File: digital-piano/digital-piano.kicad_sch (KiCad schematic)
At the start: 20 parts, among them J1 Conn_01x22, J10 Conn_01x01, J11 Conn_01x01, J12 Conn_01x01, J13 Conn_01x01, J14 Conn_01x01, J15 Conn_01x01, J16 Conn_01x01, J2 Conn_01x22, J3 Conn_01x01, J4 Conn_01x01, J5 Conn_01x01, J6 Conn_01x01, J7 Conn_01x01, J8 Conn_01x01, J9 Conn_01x01

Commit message: Assign footprints to digital-piano
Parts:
- S4: Availability In Stock -> (none); Check_prices https://www.snapeda.com/parts/SKRPACE010/ALPS/view-part/?re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 -> (none); Description_1 Switch Tactile N.O. SPST Button J-Bend 0.05A 16VDC 2.55N SM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 -> (none); MANUFACTURER ALPS -> (none); MF ALPS -> (none); MP SKRPACE010 -> (none); Package None -> (none); Price None -> (none); STANDARD Maniufacturer Recommendations -> (none); SnapEDA_Link https://www.snapeda.com/parts/SKRPACE010/ALPS/view-part/?re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 -> (none)
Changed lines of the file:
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@@
 			)
 		)
-		(property "MF" "ALPS"
+		(property "MF" ""
 			(at 232.41 114.3 0)
 			(effects
@@
 			)
 		)
-		(property "Description_1" "\n                        \n                            Switch Tactile N.O. SPST Button J-Bend 0.05A 16VDC 2.55N SMD Automotive T/R\n                        \n"
+		(property "Description_1" ""
 			(at 232.41 114.3 0)
 			(effects
@@
 			)
 		)
-		(property "Package" "None"
+		(property "Package" ""
 			(at 232.41 114.3 0)
 			(effects
@@
 			)
 		)
-		(property "Price" "None"
+		(property "Price" ""
 			(at 232.41 114.3 0)
 			(effects
@@
 			)
 		)
-		(property "Check_prices" "https://www.snapeda.com/parts/SKRPACE010/ALPS/view-part/?ref=eda"
+		(property "Check_prices" ""
 			(at 232.41 114.3 0)
 			(effects
@@
 			)
 		)
-		(property "STANDARD" "Maniufacturer Recommendations"
+		(property "STANDARD" ""
 			(at 232.41 114.3 0)
 			(effects
@@
 			)
 		)
-		(property "SnapEDA_Link" "https://www.snapeda.com/parts/SKRPACE010/ALPS/view-part/?ref=snap"
+		(property "SnapEDA_Link" ""
 			(at 232.41 114.3 0)
 			(effects
@@
 			)
 		)
-		(property "MP" "SKRPACE010"
+		(property "MP" ""
 			(at 232.41 114.3 0)
 			(effects
@@
 			)
 		)
-		(property "Availability" "In Stock"
+		(property "Availability" ""
 			(at 232.41 114.3 0)
 			(effects
@@
 			)
 		)
-		(property "MANUFACTURER" "ALPS"
+		(property "MANUFACTURER" ""
 			(at 232.41 114.3 0)
 			(effects

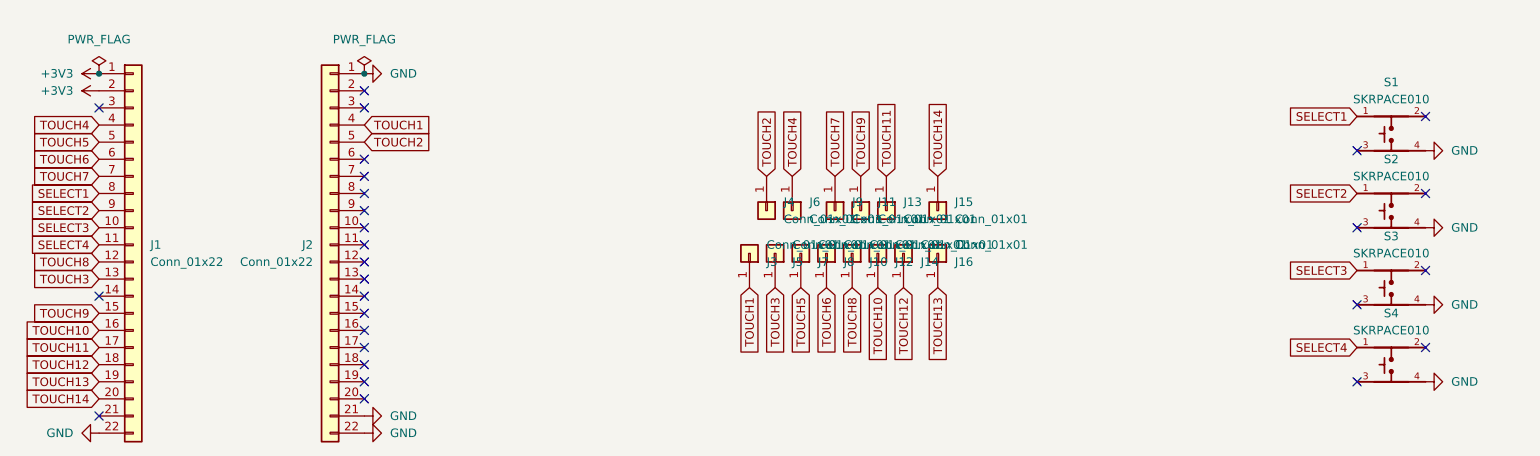
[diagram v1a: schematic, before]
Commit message: Change the name of the footprint library of touchpad
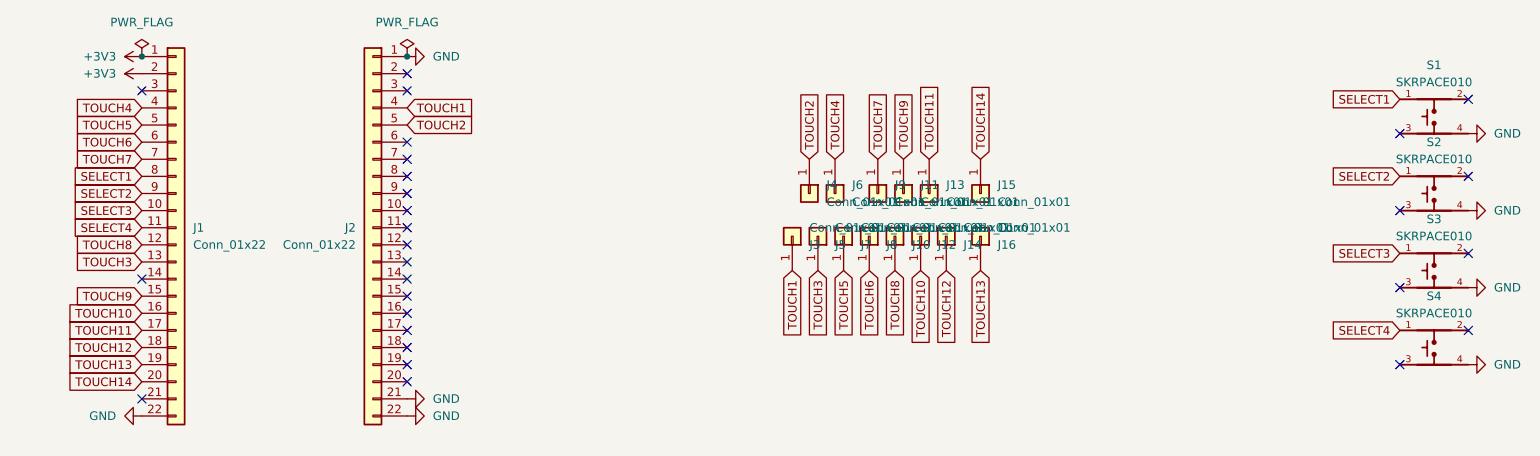
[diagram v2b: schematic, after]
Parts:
- J10, J11, J12, J13, J14, J15, J16, J3, J4, J5, J6, J7, J8, J9: footprint SparkFun-Switch:Pad-CapacitiveTouch -> Pad-CapacitiveTouch:Pad-CapacitiveTouch

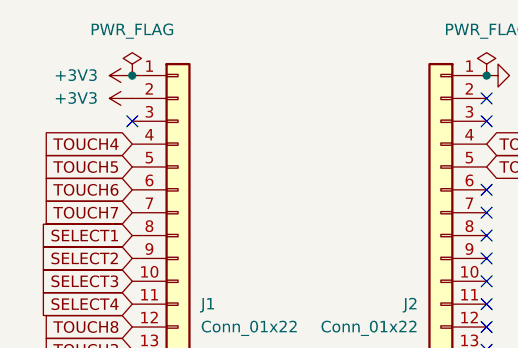
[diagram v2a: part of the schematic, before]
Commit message: Delete +3V3 from 4 dev boards
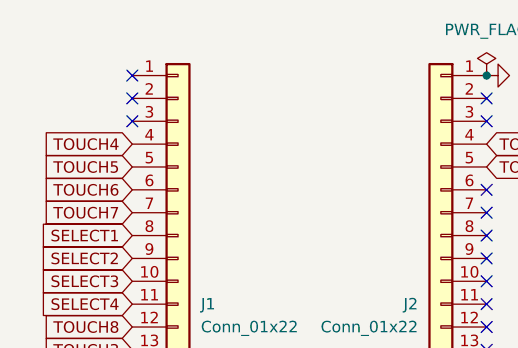
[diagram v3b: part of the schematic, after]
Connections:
- net +3V3: no longer names the net of J1.1 (Pin_1)
- net +3V3: no longer J1.2 (Pin_2)
- no-connect marks 28 -> 30
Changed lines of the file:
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@@
 		(color 0 0 0 0)
 	)
-	(junction
+	(no_connect
+		(at 86.36 116.84)
+	)
+	(no_connect
+		(at 86.36 91.44)
+	)
+	(no_connect
+		(at 46.99 119.38)
+	)
+	(no_connect
+		(at 86.36 81.28)
+	)
+	(no_connect
+		(at 86.36 93.98)
+	)
+	(no_connect
+		(at 243.84 109.22)
+	)
+	(no_connect
+		(at 86.36 83.82)
+	)
+	(no_connect
+		(at 86.36 111.76)
+	)
+	(no_connect
+		(at 46.99 101.6)
+	)
+	(no_connect
+		(at 233.68 102.87)
+	)
+	(no_connect
+		(at 243.84 97.79)
+	)
+	(no_connect
+		(at 243.84 86.36)
+	)
+	(no_connect
+		(at 233.68 91.44)
+	)
+	(no_connect
+		(at 46.99 71.12)
+	)
+	(no_connect
+		(at 86.36 99.06)
+	)
+	(no_connect
+		(at 86.36 106.68)
+	)
+	(no_connect
+		(at 86.36 114.3)
+	)
+	(no_connect
+		(at 86.36 96.52)
+	)
+	(no_connect
+		(at 86.36 109.22)
+	)
+	(no_connect
+		(at 86.36 101.6)
+	)
+	(no_connect
+		(at 86.36 88.9)
+	)
+	(no_connect
+		(at 46.99 73.66)
+	)
+	(no_connect
 		(at 46.99 68.58)
-		(diameter 0)
-		(color 0 0 0 0)
-	)
-	(no_connect
-		(at 86.36 116.84)
-	)
-	(no_connect
-		(at 86.36 91.44)
-	)
-	(no_connect
-		(at 46.99 119.38)
-	)
-	(no_connect
-		(at 86.36 81.28)
-	)
-	(no_connect
-		(at 86.36 93.98)
-	)
-	(no_connect
-		(at 243.84 109.22)
-	)
-	(no_connect
-		(at 86.36 83.82)
-	)
-	(no_connect
-		(at 86.36 111.76)
-	)
-	(no_connect
-		(at 46.99 101.6)
-	)
-	(no_connect
-		(at 233.68 102.87)
-	)
-	(no_connect
-		(at 243.84 97.79)
-	)
-	(no_connect
-		(at 243.84 86.36)
-	)
-	(no_connect
-		(at 233.68 91.44)
-	)
-	(no_connect
-		(at 86.36 99.06)
-	)
-	(no_connect
-		(at 86.36 106.68)
-	)
-	(no_connect
-		(at 86.36 114.3)
-	)
-	(no_connect
-		(at 86.36 96.52)
-	)
-	(no_connect
-		(at 86.36 109.22)
-	)
-	(no_connect
-		(at 86.36 101.6)
-	)
-	(no_connect
-		(at 86.36 88.9)
-	)
-	(no_connect
-		(at 46.99 73.66)
 	)
 	(no_connect
@@
 	)
 	(symbol
-		(lib_id "power:PWR_FLAG")
-		(at 46.99 68.58 0)
-		(unit 1)
-		(exclude_from_sim no)
-		(in_bom yes)
-		(on_board yes)
-		(dnp no)
-		(fields_autoplaced yes)
-		(property "Reference" "#FLG01"
-			(at 46.99 66.675 0)
-			(effects
-				(font
-					(size 1.27 1.27)
-				)
-				(hide yes)
-			)
-		)
-		(property "Value" "PWR_FLAG"
-			(at 46.99 63.5 0)
-			(effects
-				(font
-					(size 1.27 1.27)
-				)
-			)
-		)
-		(property "Footprint" ""
-			(at 46.99 68.58 0)
-			(effects
-				(font
-					(size 1.27 1.27)
-				)
-				(hide yes)
-			)
-		)
-		(property "Datasheet" "~"
-			(at 46.99 68.58 0)
-			(effects
-				(font
-					(size 1.27 1.27)
-				)
-				(hide yes)
-			)
-		)
-		(property "Description" "Special symbol for telling ERC where power comes from"
-			(at 46.99 68.58 0)
-			(effects
-				(font
-					(size 1.27 1.27)
-				)
-				(hide yes)
-			)
-		)
-		(pin "1"
-		)
-		(instances
-			(project "digital-piano"
-				(path "/aa27de7e-02ac-4425-b77a-ffd46d02b76f"
-					(reference "#FLG01")
-					(unit 1)
-				)
-			)
-		)
-	)
-	(symbol
 		(lib_id "Connector_Generic:Conn_01x01")
 		(at 166.37 95.25 270)
@@
 					(unit 1)
 				)
-			)
-		)
-	)
-	(symbol
-		(lib_id "power:+3V3")
-		(at 46.99 71.12 90)
-		(unit 1)
-		(exclude_from_sim no)
-		(in_bom yes)
-		(on_board yes)
-		(dnp no)
-		(fields_autoplaced yes)
-		(property "Reference" "#PWR02"
-			(at 50.8 71.12 0)
-			(effects
-				(font
-					(size 1.27 1.27)
-				)
-				(hide yes)
-			)
-		)
-		(property "Value" "+3V3"
-			(at 43.18 71.1199 90)
-			(effects
-				(font
-					(size 1.27 1.27)
-				)
-				(justify left)
-			)
-		)
-		(property "Footprint" ""
-			(at 46.99 71.12 0)
-			(effects
-				(font
-					(size 1.27 1.27)
-				)
-				(hide yes)
-			)
-		)
-		(property "Datasheet" ""
-			(at 46.99 71.12 0)
-			(effects
-				(font
-					(size 1.27 1.27)
-				)
-				(hide yes)
-			)
-		)
-		(property "Description" "Power symbol creates a global label with name \"+3V3\""
-			(at 46.99 71.12 0)
-			(effects
-				(font
-					(size 1.27 1.27)
-				)
-				(hide yes)
-			)
-		)
-		(pin "1"
-		)
-		(instances
-			(project "digital-piano"
-				(path "/aa27de7e-02ac-4425-b77a-ffd46d02b76f"
-					(reference "#PWR02")
-					(unit 1)
-				)
-			)
-		)
-	)
-	(symbol
-		(lib_id "power:+3V3")
-		(at 46.99 68.58 90)
-		(unit 1)
-		(exclude_from_sim no)
-		(in_bom yes)
-		(on_board yes)
-		(dnp no)
-		(fields_autoplaced yes)
-		(property "Reference" "#PWR01"
-			(at 50.8 68.58 0)
-			(effects
-				(font
-					(size 1.27 1.27)
-				)
-				(hide yes)
-			)
-		)
-		(property "Value" "+3V3"
-			(at 43.18 68.5799 90)
-			(effects
-				(font
-					(size 1.27 1.27)
-				)
-				(justify left)
-			)
-		)
-		(property "Footprint" ""
-			(at 46.99 68.58 0)
-			(effects
-				(font
-					(size 1.27 1.27)
-				)
-				(hide yes)
-			)
-		)
-		(property "Datasheet" ""
-			(at 46.99 68.58 0)
-			(effects
-				(font
-					(size 1.27 1.27)
-				)
-				(hide yes)
-			)
-		)
-		(property "Description" "Power symbol creates a global label with name \"+3V3\""
-			(at 46.99 68.58 0)
-			(effects
-				(font
-					(size 1.27 1.27)
-				)
-				(hide yes)
-			)
-		)
-		(pin "1"
-		)
-		(instances
-			(project "digital-piano"
-				(path "/aa27de7e-02ac-4425-b77a-ffd46d02b76f"
-					(reference "#PWR01")
-					(unit 1)
-				)
